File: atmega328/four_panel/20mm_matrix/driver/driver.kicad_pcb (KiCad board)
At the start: 2 copper layers, 40 x 40 mm, 20 parts, among them IC1 ATMEGA328-A, IC2 ATMEGA328-A, IC3 ATMEGA328-A, IC4 ATMEGA328-A, P1 CONN_2X2, P2 CONN_2X2, X1 CER_RESO, X2 CER_RESO, X3 CER_RESO, X4 CER_RESO

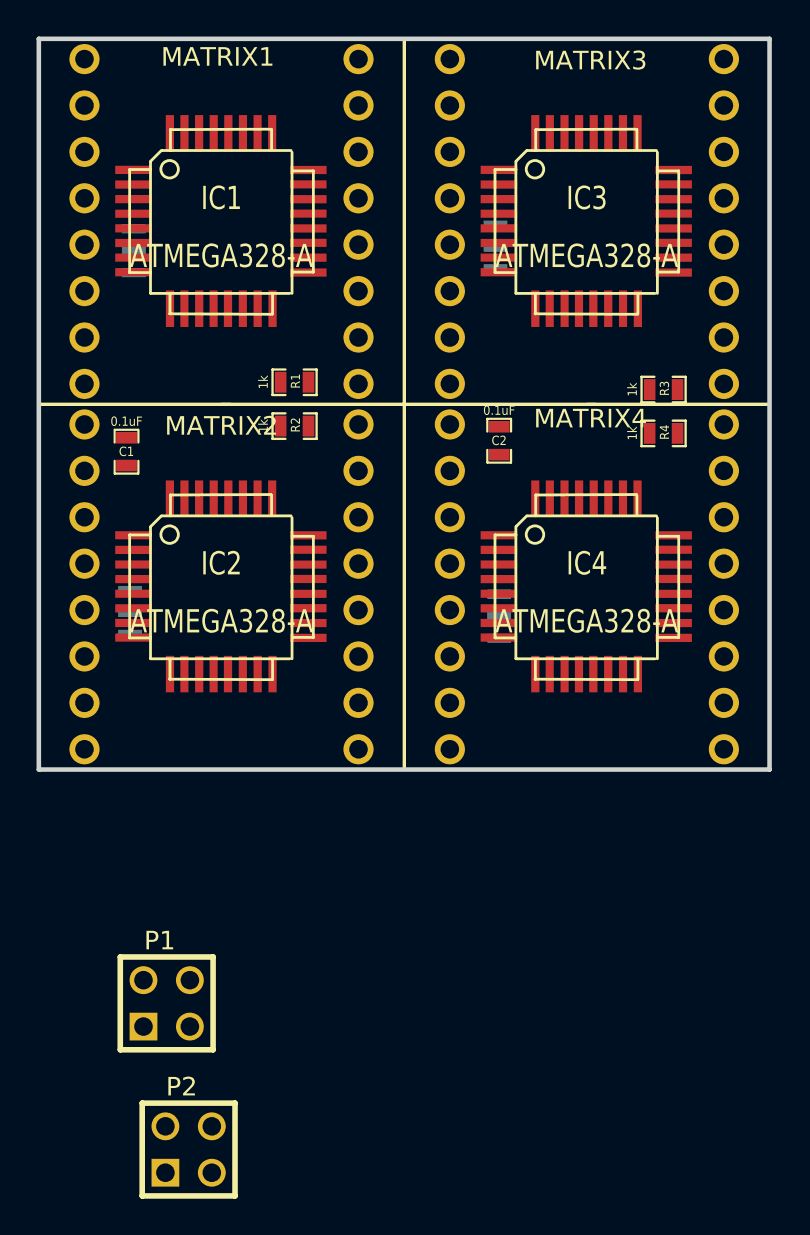
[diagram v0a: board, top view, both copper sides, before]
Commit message: Finished initial verision of four matrix atmega328 based design.
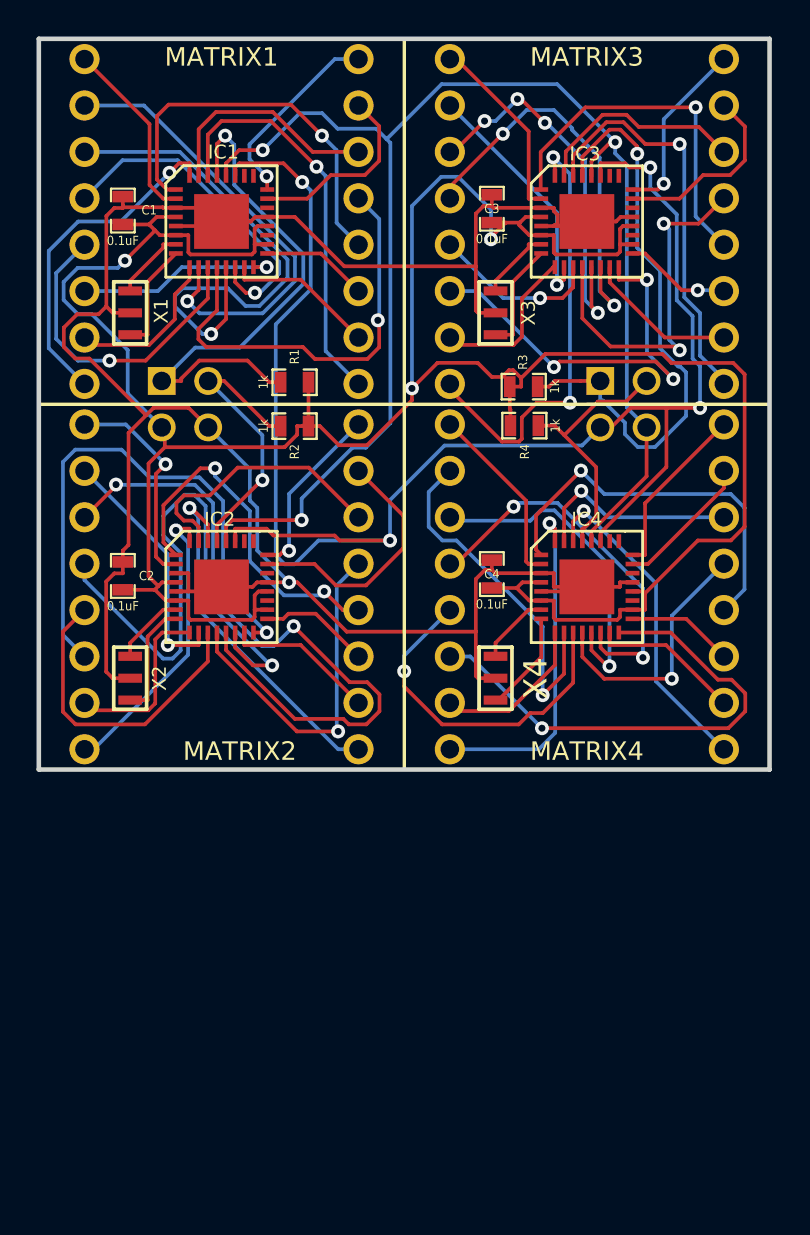
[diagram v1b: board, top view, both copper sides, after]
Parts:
- added C3: 0.1uF, SM0603_Capa, F.Cu at (74.8, 59.3)
- added C4: 0.1uF, SM0603_Capa, F.Cu at (74.8, 79.3)
- IC1, IC2, IC3, IC4: value ATMEGA328-A -> ATMEGA328P-M; footprint TQFP32 -> QFN32
- P1, P2: footprint PIN_ARRAY_2X2 -> PIN_ARRAY_F_2X2; moved to B.Cu
- X1, X2, X3, X4: moved to F.Cu
- moved P2 47.2 mm to (82.0, 70.0)
- moved P1 32.8 mm to (58.0, 70.0)
- moved C2 21.9 mm to (54.6, 79.4), turned to 90 degrees
- moved C1 13.2 mm to (54.6, 59.4), turned to 90 degrees
- moved R3 7.66 mm to (76.5, 69.0), turned to 180 degrees
- moved R4 7.63 mm to (76.6, 71.2), turned to 180 degrees
- moved X3 3.60 mm to (75.0, 65.0)
- moved X2 3.60 mm to (55.0, 85.0)
- moved X4 3.41 mm to (75.0, 85.0)
- moved X1 3.41 mm to (55.0, 65.0)
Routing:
- net +5V: track 0.00 -> 153.6 mm, vias 0 -> 3
- net GND: track 0.00 -> 130.2 mm, vias 0 -> 1
- net /SDA: track 0.00 -> 90.4 mm, vias 0 -> 4
- net /SCL: track 0.00 -> 81.1 mm, vias 0 -> 3
- net /ROW2_DRV2: track 0.00 -> 37.9 mm, vias 0 -> 2
- net /ROW3_DRV2: track 0.00 -> 32.5 mm, vias 0 -> 1
- net /RESET_DRV3: track 0.00 -> 32.4 mm, vias 0 -> 1
- net /ROW5_DRV2: track 0.00 -> 30.3 mm, vias 0 -> 1
- net /RESET_DRV1: track 0.00 -> 29.8 mm, vias 0 -> 1
- net /ROW2_DRV1: track 0.00 -> 29.1 mm, vias 0 -> 1
- net /ROW5_DRV4: track 0.00 -> 27.5 mm, vias 0 -> 1
- net /COL7_DRV1: track 0.00 -> 25.3 mm, vias 0 -> 1
- net /COL3_DRV3: track 0.00 -> 24.5 mm, vias 0 -> 2
- net /ROW1_DRV1: track 0.00 -> 23.7 mm, vias 0 -> 1
- net /ROW5_DRV3: track 0.00 -> 22.7 mm, vias 0 -> 3
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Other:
- net class Default: clearance 0.254 -> 0.2032; trace_width 0.254 -> 0.2032; via_dia 0.889 -> 0.762; via_drill 0.635 -> 0.508
- rule trace_clearance: 0.254 -> 0.2032
- rule trace_min: 0.254 -> 0.2032
- rule via_min_size: 0.889 -> 0.762

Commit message: Finished initial version of four matrix atmega328 based design.
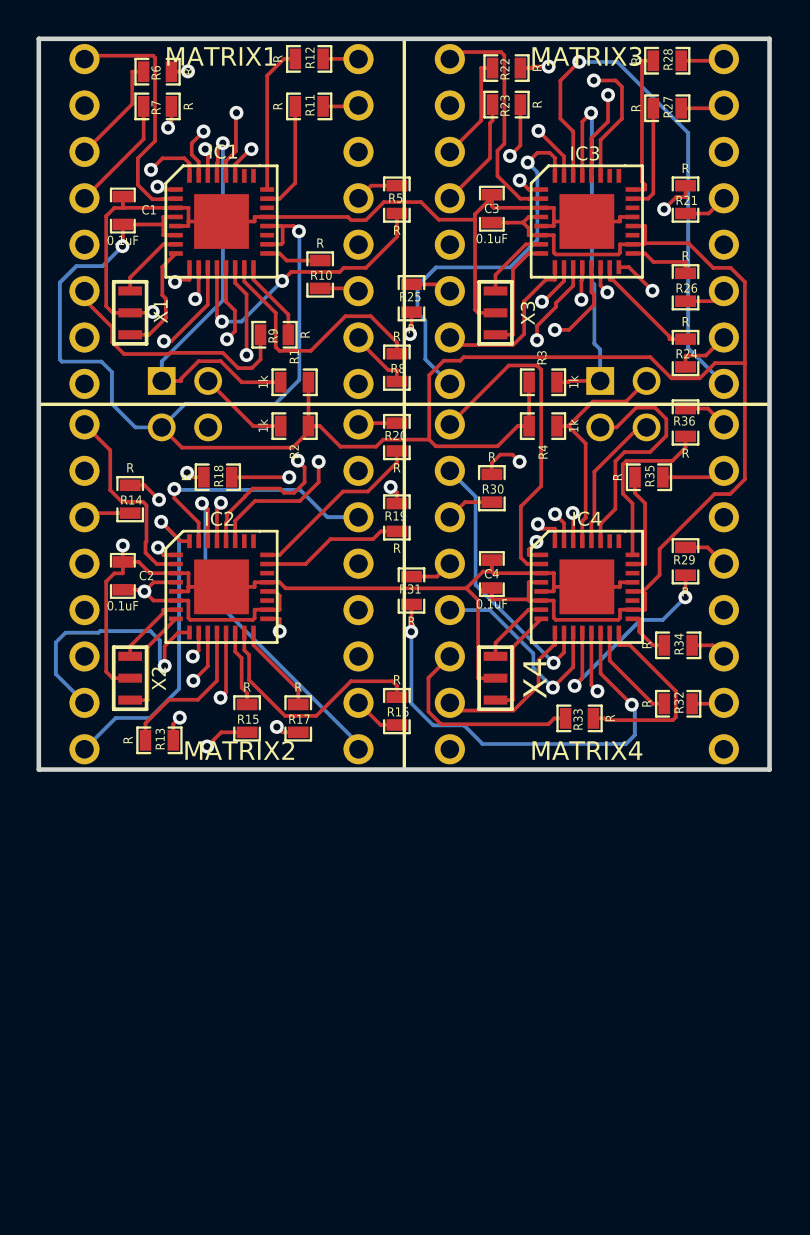
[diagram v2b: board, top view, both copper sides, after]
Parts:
- added R10: R, SM0603_Resistor, F.Cu at (65.4, 62.9)
- added R11: R, SM0603_Resistor, F.Cu at (64.8, 53.7)
- added R12: R, SM0603_Resistor, F.Cu at (64.8, 51.1)
- added R13: R, SM0603_Resistor, F.Cu at (56.6, 88.4)
- added R14: R, SM0603_Resistor, F.Cu at (55.0, 75.2)
- added R15: R, SM0603_Resistor, F.Cu at (61.4, 87.2)
- added R16: R, SM0603_Resistor, F.Cu at (69.6, 86.8)
- added R17: R, SM0603_Resistor, F.Cu at (64.2, 87.2)
- added R18: R, SM0603_Resistor, F.Cu at (59.8, 74.0)
- added R19: R, SM0603_Resistor, F.Cu at (69.6, 76.2)
- added R20: R, SM0603_Resistor, F.Cu at (69.6, 71.8)
- added R21: R, SM0603_Resistor, F.Cu at (85.4, 58.8)
- added R22: R, SM0603_Resistor, F.Cu at (75.6, 51.6)
- added R23: R, SM0603_Resistor, F.Cu at (75.6, 53.6)
- added R24: R, SM0603_Resistor, F.Cu at (85.4, 67.2)
- added R25: R, SM0603_Resistor, F.Cu at (70.4, 64.2)
- added R26: R, SM0603_Resistor, F.Cu at (85.4, 63.6)
- added R27: R, SM0603_Resistor, F.Cu at (84.4, 53.8)
- added R28: R, SM0603_Resistor, F.Cu at (84.4, 51.2)
- added R29: R, SM0603_Resistor, F.Cu at (85.4, 78.6)
- added R30: R, SM0603_Resistor, F.Cu at (74.8, 74.6)
- added R31: R, SM0603_Resistor, F.Cu at (70.4, 80.2)
- added R32: R, SM0603_Resistor, F.Cu at (85.0, 86.4)
- added R33: R, SM0603_Resistor, F.Cu at (79.6, 87.2)
- added R34: R, SM0603_Resistor, F.Cu at (85.0, 83.2)
- added R35: R, SM0603_Resistor, F.Cu at (83.4, 74.0)
- added R36: R, SM0603_Resistor, F.Cu at (85.4, 71.0)
- added R5: R, SM0603_Resistor, F.Cu at (69.6, 58.8)
- added R6: R, SM0603_Resistor, F.Cu at (56.5, 51.8)
- added R7: R, SM0603_Resistor, F.Cu at (56.5, 53.7)
- added R8: R, SM0603_Resistor, F.Cu at (69.6, 68.0)
- added R9: R, SM0603_Resistor, F.Cu at (62.9, 66.2)
- moved R3 1.08 mm to (77.6, 68.8)
- moved R4 1.02 mm to (77.6, 71.2)
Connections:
- MATRIX1 pad 10: /ROW4_DRV1 -> N-00000114
- MATRIX1 pad 11: /ROW6_DRV1 -> N-00000116
- MATRIX1 pad 13: /ROW1_DRV1 -> N-00000120
- MATRIX1 pad 15: /ROW7_DRV1 -> N-00000117
- MATRIX1 pad 16: /ROW8_DRV1 -> N-00000118
- MATRIX1 pad 3: /ROW2_DRV1 -> N-00000119
- MATRIX1 pad 4: /ROW3_DRV1 -> N-00000113
- MATRIX1 pad 6: /ROW5_DRV1 -> N-00000115
- MATRIX2 pad 10: /ROW4_DRV2 -> N-0000093
- MATRIX2 pad 11: /ROW6_DRV2 -> N-0000095
- MATRIX2 pad 13: /ROW1_DRV2 -> N-0000090
- MATRIX2 pad 15: /ROW7_DRV2 -> N-0000096
- MATRIX2 pad 16: /ROW8_DRV2 -> N-0000084
- MATRIX2 pad 3: /ROW2_DRV2 -> N-0000091
- MATRIX2 pad 4: /ROW3_DRV2 -> N-0000092
- MATRIX2 pad 6: /ROW5_DRV2 -> N-0000094
- MATRIX3 pad 10: /ROW4_DRV3 -> N-0000088
- MATRIX3 pad 11: /ROW6_DRV3 -> N-0000048
- MATRIX3 pad 13: /ROW1_DRV3 -> N-0000087
- MATRIX3 pad 15: /ROW7_DRV3 -> N-0000051
- MATRIX3 pad 16: /ROW8_DRV3 -> N-0000052
- MATRIX3 pad 3: /ROW2_DRV3 -> N-0000085
- MATRIX3 pad 4: /ROW3_DRV3 -> N-0000086
- MATRIX3 pad 6: /ROW5_DRV3 -> N-0000044
- MATRIX4 pad 10: /ROW4_DRV4 -> N-00000100
- MATRIX4 pad 11: /ROW6_DRV4 -> N-0000079
- MATRIX4 pad 13: /ROW1_DRV4 -> N-0000097
- MATRIX4 pad 15: /ROW7_DRV4 -> N-0000082
- MATRIX4 pad 16: /ROW8_DRV4 -> N-0000083
- MATRIX4 pad 3: /ROW2_DRV4 -> N-0000098
- MATRIX4 pad 4: /ROW3_DRV4 -> N-0000099
- MATRIX4 pad 6: /ROW5_DRV4 -> N-0000075
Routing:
- net /ROW3_DRV2: track 32.5 -> 4.21 mm, vias 1 -> 0
- net /ROW5_DRV2: track 30.3 -> 4.95 mm, vias 1 -> 0
- net N-0000092: track 0.00 -> 20.3 mm, vias 0 -> 1
- net /ROW2_DRV2: track 37.9 -> 17.8 mm
- net N-0000090: track 0.00 -> 18.1 mm, vias 0 -> 1
- net /ROW5_DRV4: track 27.5 -> 10.9 mm, vias 1 -> 0
- net GND: track 130.2 -> 113.8 mm, vias 1 -> 2
- net +5V: track 153.6 -> 169.3 mm
- net N-0000095: track 0.00 -> 14.5 mm, vias 0 -> 1
- net N-00000115: track 0.00 -> 13.7 mm
- net N-0000094: track 0.00 -> 13.7 mm, vias 0 -> 1
- net /COL8_DRV3: track 9.31 -> 21.7 mm
- net /RESET_DRV3: track 32.4 -> 20.9 mm
- net N-0000075: track 0.00 -> 11.4 mm
- net /ROW1_DRV2: track 19.2 -> 8.45 mm, vias 1 -> 0
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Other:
- copper layers 2 -> 4

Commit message: Modified 4 matrix atmega328 design. Added pin change interrupts and re-routed.
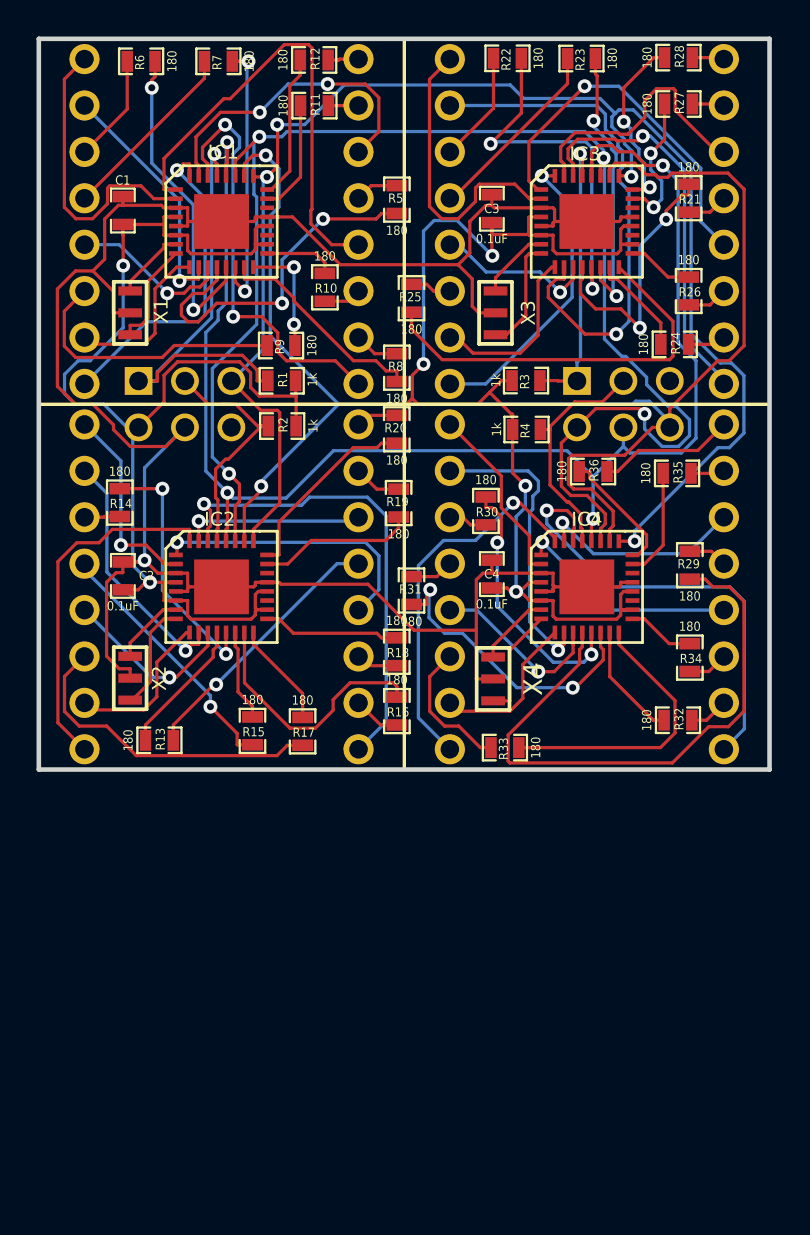
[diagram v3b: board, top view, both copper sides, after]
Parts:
- P1, P2: value CONN_2X2 -> CONN_3X2; footprint PIN_ARRAY_F_2X2 -> PIN_ARRAY_F_3X2
- R10, R11, R12, R13, R14, R15, R16, R17, R18, R19, R20, R21, R22, R23, R24, R25, R26, R27, R28, R29, R30, R31, R32, R33, R34, R35, R36, R5, R6, R7, R8, R9: value R -> 180
- moved R18 13.7 mm to (69.6, 83.6), turned to 270 degrees
- moved R36 5.73 mm to (80.3, 73.7), turned to 0 degrees
- moved R23 4.82 mm to (79.7, 51.1)
- moved R33 4.39 mm to (75.5, 88.8)
- moved R7 4.14 mm to (59.8, 51.2)
- moved R35 1.55 mm to (84.9, 73.8)
- moved R30 1.29 mm to (74.5, 75.8)
- moved R6 1.06 mm to (55.6, 51.2)
- moved R3 0.93 mm to (76.7, 68.7)
- moved R34 0.92 mm to (85.6, 83.9), turned to 270 degrees
- moved R4 0.92 mm to (76.7, 71.4)
- moved R32 0.90 mm to (85.0, 87.3)
- moved R19 0.79 mm to (69.7, 75.4)
- moved R24 0.76 mm to (84.8, 66.7), turned to 0 degrees
- moved R17 0.75 mm to (64.4, 87.9)
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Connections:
- IC1 pad 25: N-0000011 -> /PCINT10/PC2
- IC1 pad 26: N-0000013 -> /PCINT11/PC3
- IC2 pad 25: N-0000036 -> /PCINT10/PC2
- IC2 pad 26: N-0000037 -> /PCINT11/PC3
- IC3 pad 25: N-00000106 (its old number) -> /PCINT10/PC2
- IC3 pad 26: N-00000107 -> /PCINT11/PC3
- IC4 pad 25: N-00000101 (its old number) -> /PCINT10/PC2
- IC4 pad 26: N-00000102 (its old number) -> /PCINT11/PC3
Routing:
- net /PCINT10/PC2: track 0.00 -> 82.8 mm, vias 0 -> 4
- net /PCINT11/PC3: track 0.00 -> 82.5 mm, vias 0 -> 2
- net +5V: track 169.3 -> 129.9 mm, vias 3 -> 6
- net /ROW1_DRV4: track 12.4 -> 32.3 mm, vias 2 -> 0
- net /COL8_DRV3: track 21.7 -> 8.78 mm
- net /COL4_DRV1: track 13.4 -> 25.8 mm, vias 1 -> 0
- net N-00000100: track 14.5 -> 2.31 mm, vias 1 -> 0
- net /COL7_DRV3: track 16.6 -> 28.5 mm
- net /COL8_DRV1: track 17.8 -> 8.84 mm
- net /ROW3_DRV4: track 25.2 -> 16.6 mm
- net /COL5_DRV4: track 18.4 -> 10.1 mm
- net /COL1_DRV3: track 29.1 -> 21.7 mm
- net GND: track 113.8 -> 121.1 mm, vias 2 -> 1
- net /ROW3_DRV1: track 22.4 -> 15.1 mm
- net /COL1_DRV2: track 19.2 -> 26.3 mm
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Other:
- copper layers 4 -> 2
- net class Default: clearance 0.2032 -> 0.1778; trace_width 0.2032 -> 0.1778
- rule trace_clearance: 0.2032 -> 0.1778
- rule trace_min: 0.2032 -> 0.1778

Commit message: Created gerber files and BOM for 4-matrix atmega328 and max6960 PCBs.
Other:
- board text added: "4-Matrix Atmega328 Driver V1.0 www.iorodeo.com"
- board text added: "BOT"
- board text added: "K1"
- board text added: "K2"
- board text added: "K3"
- board text added: "K4"
- board text added: "K5"
- board text added: "K6"
- board text added: "K7"
- board text added: "K8"
- board text added: "TOP"
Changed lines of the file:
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@@
     (links 176)
     (no_connects 0)
-    (area 49.874999 49.874999 90.125001 90.125001)
+    (area 49.747199 49.747199 90.252801 91.763144)
     (thickness 1.6)
-    (drawings 4)
+    (drawings 15)
     (tracks 1161)
     (zones 0)
@@
     (visible_elements FFFFFF7F)
     (pcbplotparams
-      (layerselection 3178497)
+      (layerselection 284196865)
       (usegerberextensions true)
       (excludeedgelayer true)
@@
       (outputformat 1)
       (mirror false)
-      (drillshape 1)
+      (drillshape 0)
       (scaleselection 1)
-      (outputdirectory ""))
+      (outputdirectory gerber_v0p1/))
   )
   (net 0 "")
@@
     )
   )
+  (gr_text BOT (at 84.9122 89.0778) (layer B.SilkS)
+    (effects (font (size 1.016 1.016) (thickness 0.2032)) (justify mirror))
+  )
+  (gr_text TOP (at 84.9249 51.1302) (layer B.SilkS)
+    (effects (font (size 1.016 1.016) (thickness 0.2032)) (justify mirror))
+  )
+  (gr_text K8 (at 89.2175 89.0524 90) (layer F.SilkS)
+    (effects (font (size 0.889 0.889) (thickness 0.2032)))
+  )
+  (gr_text K7 (at 70.8787 89.027 90) (layer F.SilkS)
+    (effects (font (size 0.889 0.889) (thickness 0.2032)))
+  )
+  (gr_text K6 (at 89.2429 51.0413 90) (layer F.SilkS)
+    (effects (font (size 0.889 0.889) (thickness 0.2032)))
+  )
+  (gr_text K5 (at 70.866 50.9905 90) (layer F.SilkS)
+    (effects (font (size 0.889 0.889) (thickness 0.2032)))
+  )
+  (gr_text K4 (at 69.2531 89.027 90) (layer F.SilkS)
+    (effects (font (size 0.889 0.889) (thickness 0.2032)))
+  )
+  (gr_text K3 (at 50.8127 88.8492 90) (layer F.SilkS)
+    (effects (font (size 0.889 0.889) (thickness 0.2032)))
+  )
+  (gr_text K2 (at 69.1642 50.9524 90) (layer F.SilkS)
+    (effects (font (size 0.889 0.889) (thickness 0.2032)))
+  )
+  (gr_text K1 (at 50.8 50.9778 90) (layer F.SilkS)
+    (effects (font (size 0.889 0.889) (thickness 0.2032)))
+  )
+  (gr_text "4-Matrix Atmega328 Driver V1.0\nwww.iorodeo.com" (at 63.5 70 90) (layer B.SilkS)
+    (effects (font (size 1.016 1.016) (thickness 0.2032)) (justify mirror))
+  )
   (gr_line (start 90 90) (end 90 50) (angle 90) (layer Edge.Cuts) (width 0.25))
